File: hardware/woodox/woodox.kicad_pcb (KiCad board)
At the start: 4 copper layers, 162.2 x 126.5 mm, 233 parts, among them J1 Conn_01x03_Female, J10 Conn_01x01, J11 Conn_01x01, J12 Conn_01x01, J2 USB_C_To_Host, J3 Conn_01x03_Female, J4 USB_C_To_Host, J5 Conn_01x05_Socket, J6 USB_C_Interlink, J7 USB_C_Interlink, J8 Conn_01x05_Socket, J9 Conn_01x01, SW1 SW_Push, SW2 SW_Push, SW3 SW_Push, SW4 SW_Push, U1 DRV5057A3, U10 OLED_256x64_I2C, U11 DRV5057A3, U12 DRV5057A3, U13 DRV5057A3, U14 DRV5057A3, U15 DRV5057A3, U16 DRV5057A3, U17 DRV5057A3, U18 DRV5057A3, U19 DRV5057A3, U2 DRV5057A3, U20 DRV5057A3, U21 DRV5057A3, U22 DRV5057A3, U23 DRV5057A3, U24 DRV5057A3, U25 W25Q128JVP, U26 DRV5057A3, U27 DRV5057A3, U28 DRV5057A3, U29 DRV5057A3, U3 DRV5057A3, U30 DRV5057A3, U31 DRV5057A3, U32 DRV5057A3, U33 NCP1117-3.3_SOT223, U34 74HC4051, U35 74HC4051, U36 74HC4051, U37 74HC4051, U38 DRV5057A3, U39 DRV5057A3, U4 DRV5057A3, U40 DRV5057A3, U41 DRV5057A3, U42 DRV5057A3, U43 DRV5057A3, U44 DRV5057A3, U45 DRV5057A3, U46 DRV5057A3, U47 DRV5057A3, U48 DRV5057A3, U49 W25Q128JVP, U5 DRV5057A3, U50 DRV5057A3, U51 DRV5057A3, U52 DRV5057A3, U53 DRV5057A3, U54 DRV5057A3, U55 DRV5057A3, U56 DRV5057A3, U57 DRV5057A3, U58 DRV5057A3, U59 DRV5057A3, U6 DRV5057A3, U60 DRV5057A3, U61 DRV5057A3, U62 DRV5057A3, U63 DRV5057A3, U64 RP2350_80QFN, U65 DRV5057A3, U66 DRV5057A3, U67 DRV5057A3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

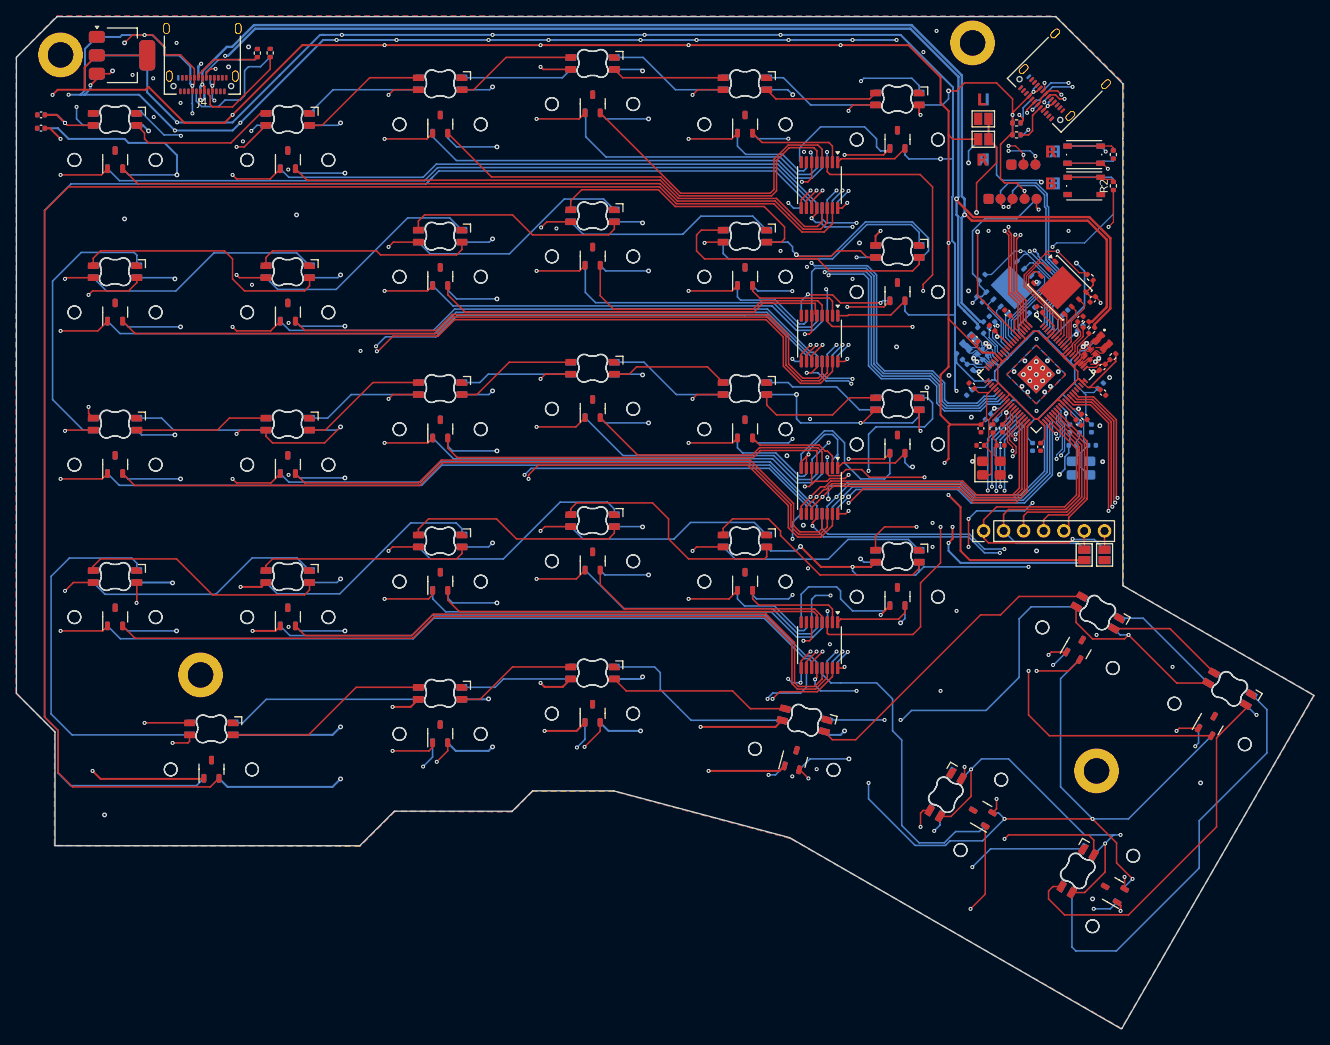
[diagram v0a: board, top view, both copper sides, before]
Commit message: adjust led footprint and board outline
only minor adjustments for step export to make a clean closing outline
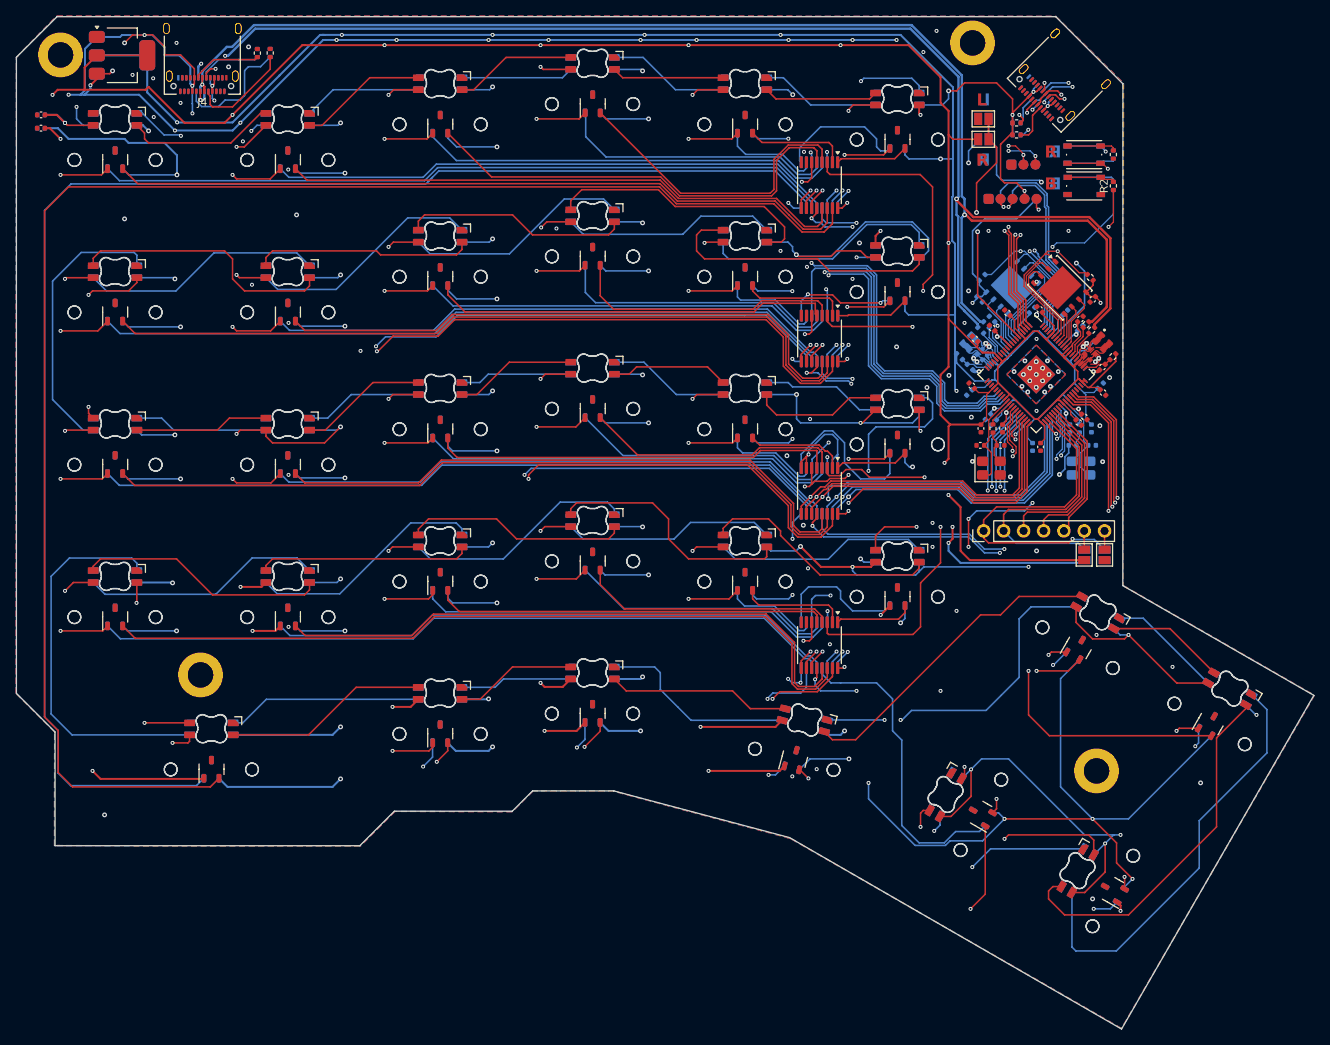
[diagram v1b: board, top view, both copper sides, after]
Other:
- outline, holes or cut-outs redrawn
